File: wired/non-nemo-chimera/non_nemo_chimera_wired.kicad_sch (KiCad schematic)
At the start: 84 parts

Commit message: Updated cases for Chimera Wired
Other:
- title: Non Nemo Chimera -> Non Nemo Chimera Wired
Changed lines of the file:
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@@
 	(paper "A3")
 	(title_block
-		(title "Non Nemo Chimera")
-		(date "2025-04-09")
+		(title "Non Nemo Chimera Wired")
+		(date "2025-04-21")
 		(rev "0.2.0")
 	)

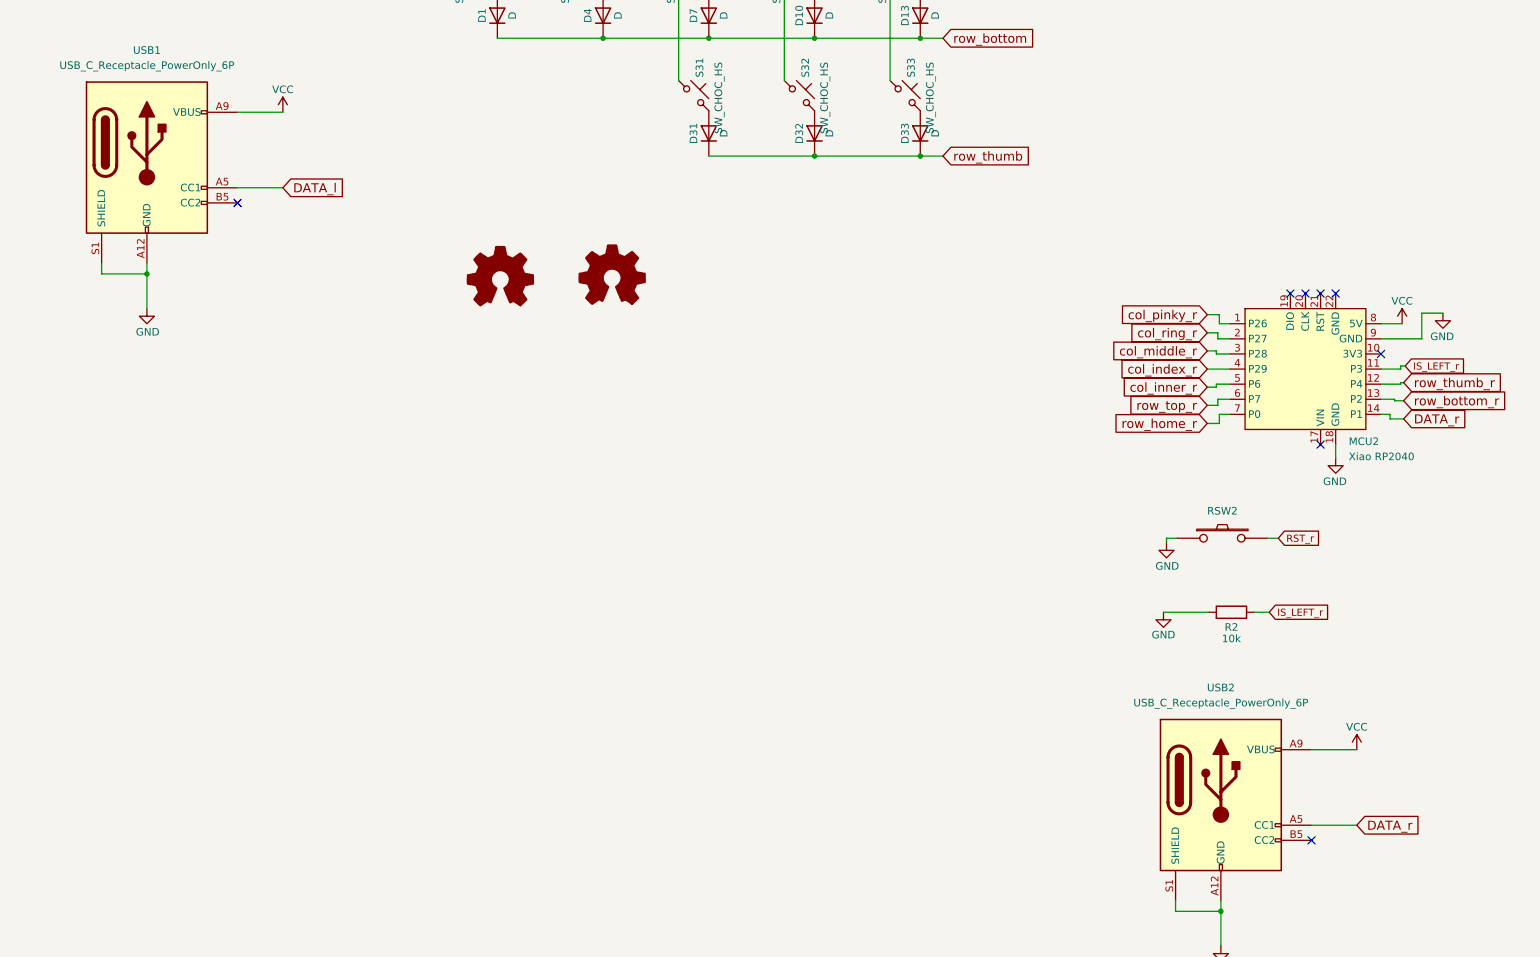
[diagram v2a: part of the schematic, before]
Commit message: fixed Wired (#12)
* fixed Non Nemo Wired

* fixed ergogen for Wired
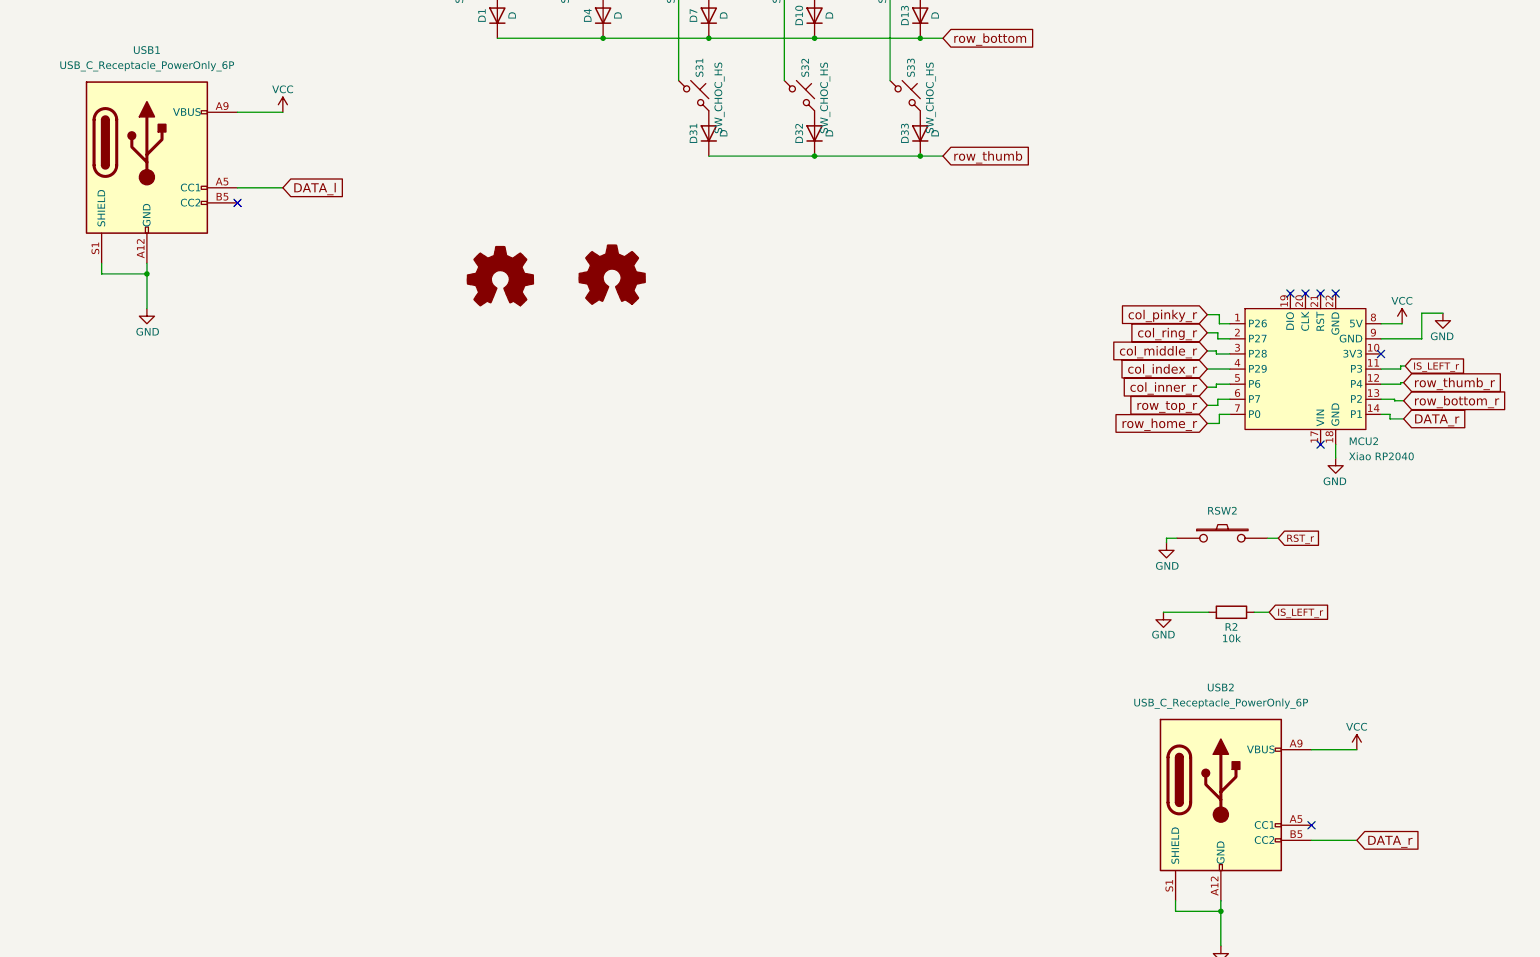
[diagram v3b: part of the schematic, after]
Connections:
- net DATA_r: now also USB2.B5 (CC2); no longer USB2.A5 (CC1)
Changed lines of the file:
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@@
 (kicad_sch
-	(version 20231120)
+	(version 20250114)
 	(generator "eeschema")
-	(generator_version "8.0")
+	(generator_version "9.0")
 	(paper "A3")
 	(title_block
@@
 	)
 	(no_connect
-		(at 235.458 234.188)
+		(at 235.458 231.648)
 	)
 	(no_connect
@@
 	(wire
 		(pts
-			(xy 243.078 231.648) (xy 235.458 231.648)
-		)
-		(stroke
-			(width 0)
-			(type default)
-		)
-	)
-	(wire
-		(pts
 			(xy 309.118 195.58) (xy 326.898 195.58)
 		)
@@
 	(wire
 		(pts
+			(xy 235.458 234.188) (xy 243.078 234.188)
+		)
+		(stroke
+			(width 0)
+			(type default)
+		)
+	)
+	(wire
+		(pts
 			(xy 29.21 73.66) (xy 29.972 73.66)
 		)
@@
 	(global_label "DATA_r"
 		(shape input)
-		(at 243.078 231.648 0)
+		(at 243.078 234.188 0)
 		(fields_autoplaced yes)
 		(effects
@@
 		)
 		(property "Intersheetrefs" "${INTERSHEET_REFS}"
-			(at 254.0619 231.648 0)
+			(at 254.0619 234.188 0)
 			(effects
 				(font
@@
 		)
 	)
+	(embedded_fonts no)
 )
